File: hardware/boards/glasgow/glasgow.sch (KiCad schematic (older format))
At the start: 95 parts, among them J1 USB_C_USB2.0, SW1 RST, U1 CY7C68013A-56LTX, U15 TPD3S014, U2 CAT24M01X, U3 BL24C256A-SFRC, U30 ICE40HX8K-BG121, U36 TLV73312PQDRVRQ1, U7 APX811-40UG-7, U8 TLV75533PDRVR, Y1 24M

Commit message: revC2: Improved anchor of the tact switch shield to the PCB.
We now have through hole slots that will solder to the metal shield tabs
of the tact switch. This will securely anchor the tact switch to the
PCB.
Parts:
- SW1: symbol Switch:SW_Push -> Glasgow:SW_Push_Shield
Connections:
- new net SWSH: SW1.3
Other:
- moved on the sheet: C89
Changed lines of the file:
@@
 L power:GND #PWR035
 U 1 1 5B2A0BF8
-P 8700 4400
-F 0 "#PWR035" H 8700 4150 50  0001 C CNN
-F 1 "GND" H 8705 4227 50  0000 C CNN
-F 2 "" H 8700 4400 50  0001 C CNN
-F 3 "" H 8700 4400 50  0001 C CNN
-	1    8700 4400
+P 8700 4500
+F 0 "#PWR035" H 8700 4250 50  0001 C CNN
+F 1 "GND" H 8705 4327 50  0000 C CNN
+F 2 "" H 8700 4500 50  0001 C CNN
+F 3 "" H 8700 4500 50  0001 C CNN
+	1    8700 4500
 	1    0    0    -1
 $EndComp
@@
 	8300 3600 8100 3600
 $Comp
-L Switch:SW_Push SW1
+L Glasgow:SW_Push_Shield SW1
 U 1 1 5F4ADDEF
 P 8400 4100
@@
 L Device:C C89
 U 1 1 5F4262BE
-P 8400 4300
-F 0 "C89" V 8350 4500 50  0000 C CNN
-F 1 "u1" V 8350 4100 50  0000 C CNN
-F 2 "Capacitor_SMD:C_0402_1005Metric" H 8438 4150 50  0001 C CNN
-F 3 "https://www.mouser.com/datasheet/2/396/mlcc02_e-1307760.pdf" H 8400 4300 50  0001 C CNN
-F 4 "Taiyo Yuden" H 1400 2900 50  0001 C CNN "Mfg"
-F 5 "TMK105BJ104KV-F" H 1400 2900 50  0001 C CNN "MPN"
-F 6 "cap-cer-0402-100n" H 8400 4300 50  0001 C CNN "1b2-bom-key"
-	1    8400 4300
-	0    -1   1    0
+P 8100 4350
+F 0 "C89" H 8250 4450 50  0000 R CNN
+F 1 "u1" H 8200 4250 50  0000 R CNN
+F 2 "Capacitor_SMD:C_0402_1005Metric" H 8138 4200 50  0001 C CNN
+F 3 "https://www.mouser.com/datasheet/2/396/mlcc02_e-1307760.pdf" H 8100 4350 50  0001 C CNN
+F 4 "Taiyo Yuden" H 1100 2950 50  0001 C CNN "Mfg"
+F 5 "TMK105BJ104KV-F" H 1100 2950 50  0001 C CNN "MPN"
+F 6 "cap-cer-0402-100n" H 8100 4350 50  0001 C CNN "1b2-bom-key"
+	1    8100 4350
+	-1   0    0    -1
 $EndComp
 Wire Wire Line
-	8550 4300 8700 4300
-Wire Wire Line
-	8700 4300 8700 4400
-Wire Wire Line
 	8700 3900 8700 4100
-Connection ~ 8700 4300
 Wire Wire Line
 	8600 4100 8700 4100
 Connection ~ 8700 4100
-Wire Wire Line
-	8700 4100 8700 4300
-Wire Wire Line
-	8250 4300 8100 4300
 Wire Wire Line
 	8100 3600 8100 4100
@@
 Connection ~ 8100 4100
 Wire Wire Line
-	8100 4100 8100 4300
+	8100 4100 8100 4200
 Text Notes 8050 5250 0    50   ~ 0
 A reset of U1 switches off \nthe Vio regulators due to \npulldowns. The RST button\nis designed to be usable \nas emergency off button.
 Text Notes 8850 4700 0    50   ~ 0
 Cycle +3.3V\non reset to \nget I2C peri-\npherals into \nclean state.
+Wire Wire Line
+	8700 4100 8700 4500
+$Comp
+L power:GND #PWR?
+U 1 1 5F620C92
+P 8100 4500
+F 0 "#PWR?" H 8100 4250 50  0001 C CNN
+F 1 "GND" H 8105 4327 50  0000 C CNN
+F 2 "" H 8100 4500 50  0001 C CNN
+F 3 "" H 8100 4500 50  0001 C CNN
+	1    8100 4500
+	1    0    0    -1
+$EndComp
+Wire Wire Line
+	8400 4200 8400 4300
+Text Label 8400 4300 3    50   ~ 0
+SWSH
 Wire Bus Line
 	4700 6250 7850 6250

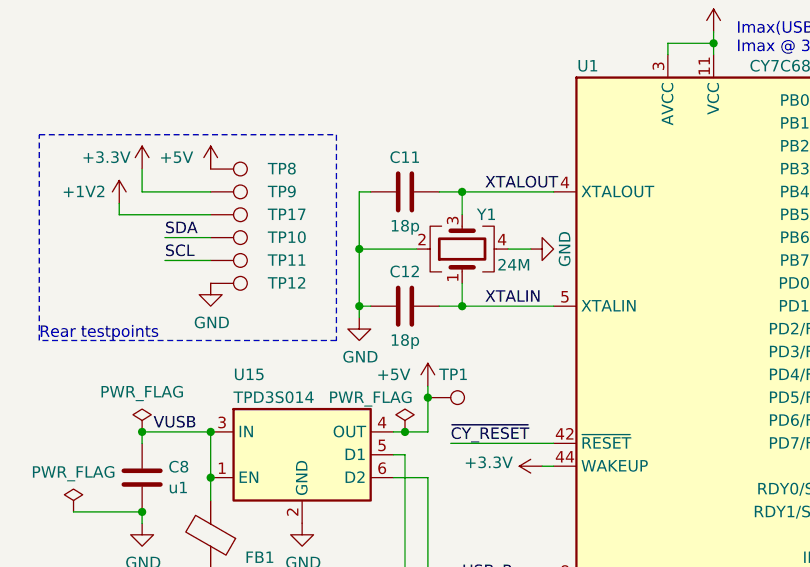
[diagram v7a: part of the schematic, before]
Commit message: revC2: Updated 1b2-bom-keys and corrected levelshifter PN.
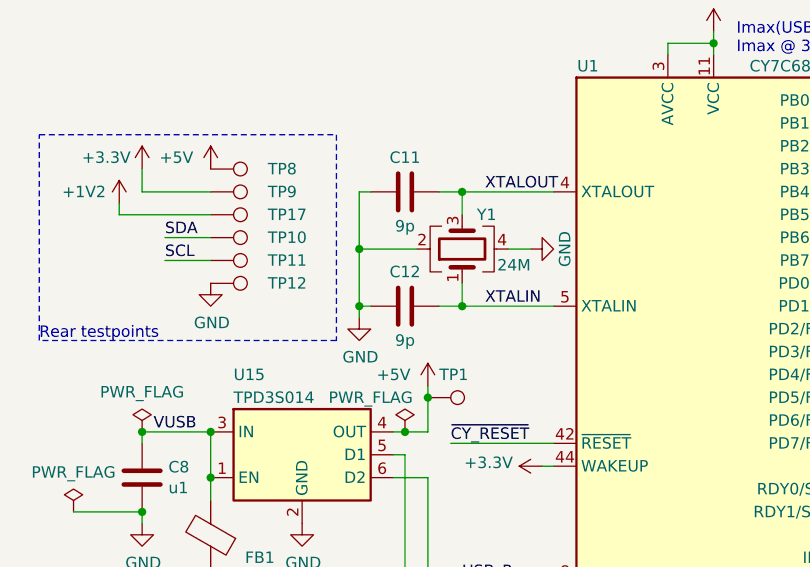
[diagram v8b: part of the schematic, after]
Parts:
- C11, C12: value 18p -> 9p; 1b2-bom-key cap-cer-0402-18p -> cap-cer-0402-9p; MPN CC0402JRNPO8BN180 -> AC0402CRNPO9BN9R0
- C87: 1b2-bom-key cap-poly-6_3x6_0-10v-150u -> cap-poly-6_3x5_7-10v-150u
- D24: 1b2-bom-key (none) -> diode-sot323-bat54aw
- J1: 1b2-bom-key (none) -> conn-smd-usb-c-2; MPN (none) -> TYPE-C-31-M-12; Mfg (none) -> Korean Hroparts Elec
- SW1: 1b2-bom-key ??? -> sw-tact-side-1ts003a
- U36: 1b2-bom-key ic-dfn6-tlv73312pqrdvrq1 -> vreg-dfn6-tlv73312pqrdvrq1
- U8: 1b2-bom-key ic-dfn6-tlv75533pdrvr -> vreg-dfn6-tlv75533pdrvr
- Y1: 1b2-bom-key xtal-lfxtal-24mhz -> xtal-smd3225-24mhz-9p; Characteristics (none) -> 9pF load; MPN LFXTAL058124REEL -> JF4024M00009T8188070; Mfg IQD -> JWT
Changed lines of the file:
@@
 P 2200 2450
 F 0 "C11" V 2050 2450 50  0000 C CNN
-F 1 "18p" V 2350 2450 50  0000 C CNN
+F 1 "9p" V 2350 2450 50  0000 C CNN
 F 2 "Capacitor_SMD:C_0402_1005Metric" H 2238 2300 50  0001 C CNN
-F 3 "https://www.mouser.com/datasheet/2/447/UPY-GP_NP0_16V-to-50V_16-1109089.pdf" H 2200 2450 50  0001 C CNN
+F 3 "https://www.mouser.com/datasheet/2/447/Yageo_UPY-AC_NP0X7R_16V-to-630V_12-1827077-1874686.pdf" H 2200 2450 50  0001 C CNN
 F 4 "Yageo" H 650 -250 50  0001 C CNN "Mfg"
-F 5 "CC0402JRNPO8BN180" H 650 -250 50  0001 C CNN "MPN"
-F 6 "cap-cer-0402-18p" H 2200 2450 50  0001 C CNN "1b2-bom-key"
+F 5 "AC0402CRNPO9BN9R0" H 650 -250 50  0001 C CNN "MPN"
+F 6 "cap-cer-0402-9p" H 2200 2450 50  0001 C CNN "1b2-bom-key"
 	1    2200 2450
 	0    1    1    0
@@
 P 2200 2950
 F 0 "C12" V 2050 2950 50  0000 C CNN
-F 1 "18p" V 2350 2950 50  0000 C CNN
+F 1 "9p" V 2350 2950 50  0000 C CNN
 F 2 "Capacitor_SMD:C_0402_1005Metric" H 2238 2800 50  0001 C CNN
-F 3 "https://www.mouser.com/datasheet/2/447/UPY-GP_NP0_16V-to-50V_16-1109089.pdf" H 2200 2950 50  0001 C CNN
+F 3 "https://www.mouser.com/datasheet/2/447/Yageo_UPY-AC_NP0X7R_16V-to-630V_12-1827077-1874686.pdf" H 2200 2950 50  0001 C CNN
 F 4 "Yageo" H 650 -250 50  0001 C CNN "Mfg"
-F 5 "CC0402JRNPO8BN180" H 650 -250 50  0001 C CNN "MPN"
-F 6 "cap-cer-0402-18p" H 2200 2950 50  0001 C CNN "1b2-bom-key"
+F 5 "AC0402CRNPO9BN9R0" H 650 -250 50  0001 C CNN "MPN"
+F 6 "cap-cer-0402-9p" H 2200 2950 50  0001 C CNN "1b2-bom-key"
 	1    2200 2950
 	0    1    1    0
@@
 F 1 "24M" V 2350 2400 50  0000 L TNN
 F 2 "Glasgow:Crystal_SMD_3225-4Pin_3.2x2.5mm" H 2450 2700 50  0001 C CNN
-F 3 "https://www.mouser.com/datasheet/2/741/LFXTAL058124Reel-940455.pdf" H 2450 2700 50  0001 C CNN
-F 4 "IQD" H 650 -250 50  0001 C CNN "Mfg"
-F 5 "LFXTAL058124REEL" H 650 -250 50  0001 C CNN "MPN"
-F 6 "xtal-lfxtal-24mhz" H 2450 2700 50  0001 C CNN "1b2-bom-key"
+F 3 "https://datasheet.lcsc.com/szlcsc/2008211535_JWT-JF4024M00009T8188070_C709181.pdf" H 2450 2700 50  0001 C CNN
+F 4 "JWT" H 650 -250 50  0001 C CNN "Mfg"
+F 5 "JF4024M00009T8188070" H 650 -250 50  0001 C CNN "MPN"
+F 6 "xtal-smd3225-24mhz-9p" H 2450 2700 50  0001 C CNN "1b2-bom-key"
+F 7 "9pF load" H 2450 2700 50  0001 C CNN "Characteristics"
 	1    2450 2700
 	0    -1   -1   0
@@
 F 2 "Glasgow:DFN-6-1EP_2x2mm_P0.65mm_EP1x1.6mm_ThermalVias" H 9900 5075 50  0001 C CIN
 F 3 "http://www.ti.com/lit/ds/symlink/tlv733p-q1.pdf" H 9900 4800 50  0001 C CNN
-F 4 "ic-dfn6-tlv75533pdrvr" H 9900 4750 50  0001 C CNN "1b2-bom-key"
+F 4 "vreg-dfn6-tlv75533pdrvr" H 9900 4750 50  0001 C CNN "1b2-bom-key"
 F 5 "TLV75533PDRVR" H 9900 4750 50  0001 C CNN "MPN"
 F 6 "Texas Instruments" H 9900 4750 50  0001 C CNN "Mfg"
@@
 F 2 "Glasgow:DFN-6-1EP_2x2mm_P0.65mm_EP1x1.6mm_ThermalVias" H 9900 6125 50  0001 C CIN
 F 3 "http://www.ti.com/lit/ds/symlink/tlv755p.pdf" H 9900 5850 50  0001 C CNN
-F 4 "ic-dfn6-tlv73312pqrdvrq1" H 9900 5800 50  0001 C CNN "1b2-bom-key"
+F 4 "vreg-dfn6-tlv73312pqrdvrq1" H 9900 5800 50  0001 C CNN "1b2-bom-key"
 F 5 "TLV73312PQDRVRQ1" H 9900 5800 50  0001 C CNN "MPN"
 F 6 "Texas Instruments" H 9900 5800 50  0001 C CNN "Mfg"
@@
 F 4 "A765EB157M1ALAE022" H 8150 5750 50  0001 C CNN "MPN"
 F 5 "KEMET" H 8150 5750 50  0001 C CNN "Mfg"
-F 6 "cap-poly-6_3x6_0-10v-150u" H 8150 5750 50  0001 C CNN "1b2-bom-key"
+F 6 "cap-poly-6_3x5_7-10v-150u" H 8150 5750 50  0001 C CNN "1b2-bom-key"
 F 7 "10V" H 8150 5750 50  0001 C CNN "Characteristics"
 	1    8150 5750
@@
 F 2 "Glasgow:USB_C_Receptacle_HRO_TYPE-C-31-M-12" H 1050 4950 50  0001 C CNN
 F 3 "https://www.usb.org/sites/default/files/documents/usb_type-c.zip" H 1050 4950 50  0001 C CNN
+F 4 "conn-smd-usb-c-2" H 900 4950 50  0001 C CNN "1b2-bom-key"
+F 5 "TYPE-C-31-M-12" H 900 4950 50  0001 C CNN "MPN"
+F 6 "Korean Hroparts Elec" H 900 4950 50  0001 C CNN "Mfg"
 	1    900  4950
 	1    0    0    -1
@@
 F 4 "BAT54AW-7-F" V 9950 3900 50  0001 C CNN "MPN"
 F 5 "Diodes Inc." V 9950 3900 50  0001 C CNN "Mfg"
+F 6 "diode-sot323-bat54aw" H 9950 3900 50  0001 C CNN "1b2-bom-key"
 	1    9950 3900
 	0    -1   -1   0
@@
 F 4 "HYP (Hongyuan Precision)" H 8400 4100 50  0001 C CNN "Mfg"
 F 5 "1TS003A-1600-3500A-CT" H 8400 4100 50  0001 C CNN "MPN"
-F 6 "???" H 8400 4100 50  0001 C CNN "1b2-bom-key"
+F 6 "sw-tact-side-1ts003a" H 8400 4100 50  0001 C CNN "1b2-bom-key"
 	1    8400 4100
 	-1   0    0    -1
@@
 	8700 4100 8700 4500
 $Comp
-L power:GND #PWR?
+L power:GND #PWR0199
 U 1 1 5F620C92
 P 8100 4500
-F 0 "#PWR?" H 8100 4250 50  0001 C CNN
+F 0 "#PWR0199" H 8100 4250 50  0001 C CNN
 F 1 "GND" H 8105 4327 50  0000 C CNN
 F 2 "" H 8100 4500 50  0001 C CNN
